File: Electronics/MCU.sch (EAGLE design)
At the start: 37 parts, among them IC2 74AC157D, J77 uart, U1 ATMEGA2560-16AU-TQFP100, U2 AT25DF041A-SH-B

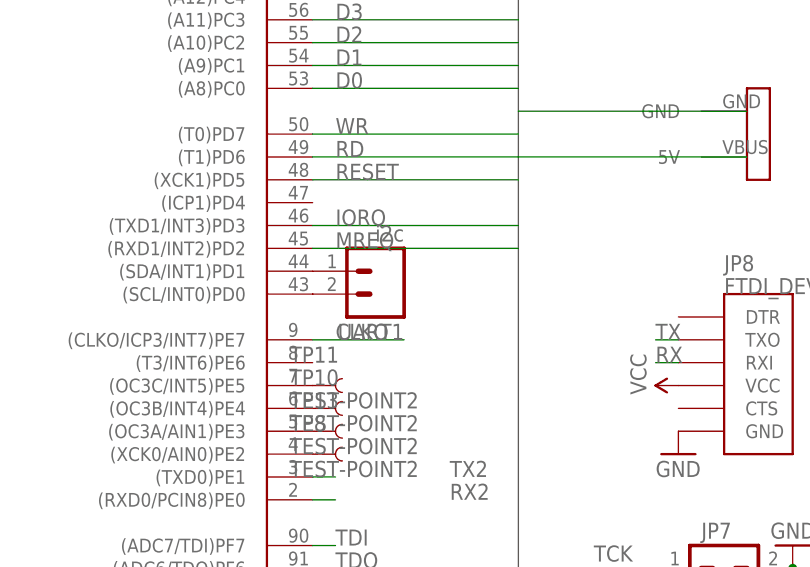
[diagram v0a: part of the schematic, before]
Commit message: Expanding bus driver
Added basic features to control the bus lines
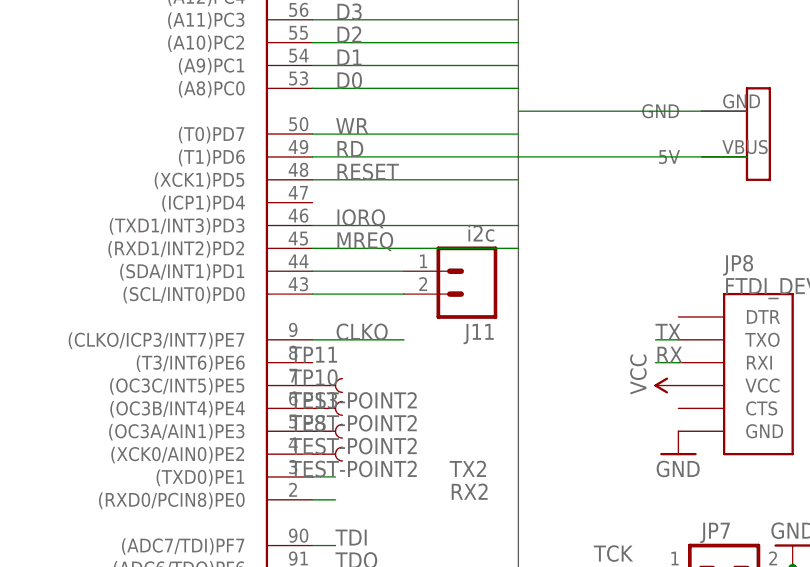
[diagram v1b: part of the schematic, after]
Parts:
- removed UART1: i2c, SparkFun:M02PTH
- added J11: i2c, SparkFun:M02PTH
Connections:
- net N$3: now also J11.1; no longer UART1.1
- net N$4: now also J11.2; no longer UART1.2
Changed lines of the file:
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@@
 <part name="P+11" library="SparkFun" deviceset="VCC" device=""/>
 <part name="J77" library="SparkFun" deviceset="M02" device="PTH" value="uart"/>
-<part name="UART1" library="SparkFun" deviceset="M02" device="PTH" value="i2c"/>
+<part name="J11" library="SparkFun" deviceset="M02" device="PTH" value="i2c"/>
 <part name="C1" library="rcl" deviceset="C-EU" device="C0805"/>
 <part name="C2" library="rcl" deviceset="C-EU" device="C0805"/>
@@
 <instance part="P+11" gate="1" x="142.24" y="-71.12" rot="R90"/>
 <instance part="J77" gate="G$1" x="22.86" y="-66.04"/>
-<instance part="UART1" gate="G$1" x="109.22" y="0" rot="R180"/>
+<instance part="J11" gate="G$1" x="119.38" y="0" rot="R180"/>
 <instance part="C1" gate="G$1" x="129.54" y="93.98"/>
 <instance part="C2" gate="G$1" x="134.62" y="93.98"/>
@@
 <segment>
 <pinref part="U1" gate="1" pin="(SDA/INT1)PD1"/>
-<pinref part="UART1" gate="G$1" pin="1"/>
+<pinref part="J11" gate="G$1" pin="1"/>
+<wire x1="111.76" y1="0" x2="101.6" y2="0" width="0.1524" layer="91"/>
 </segment>
 </net>
@@
 <segment>
 <pinref part="U1" gate="1" pin="(SCL/INT0)PD0"/>
-<pinref part="UART1" gate="G$1" pin="2"/>
-</segment>
-</net>
+<pinref part="J11" gate="G$1" pin="2"/>
+<wire x1="111.76" y1="-2.54" x2="101.6" y2="-2.54" width="0.1524" layer="91"/>
+</segment>
+</net>
